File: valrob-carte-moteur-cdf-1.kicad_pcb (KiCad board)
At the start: 2 copper layers, 63 x 50 mm, 89 parts, among them J1 USB_C_Receptacle_USB2.0_14P, J2 Conn_01x02, J3 Conn_01x02, J4 Conn_01x04_Pin, J5 Conn_01x08, J6 Conn_01x02, J7 Conn_01x02, J8 Conn_01x08, J9 Conn_01x04_Pin, SW1 SW_Push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

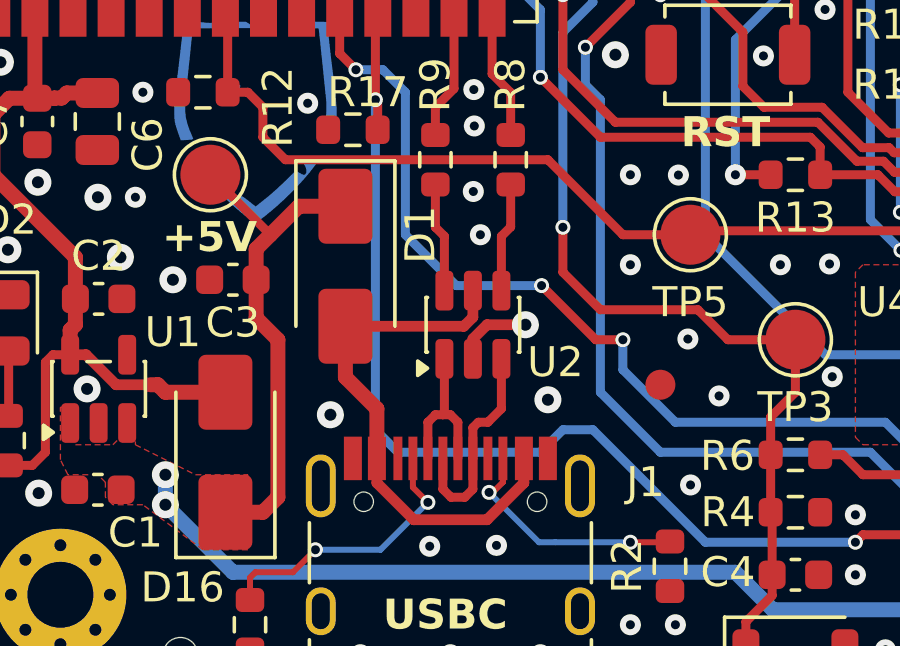
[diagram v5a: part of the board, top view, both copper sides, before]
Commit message: switch ST usb ESD to H5VU10U tvs diodes
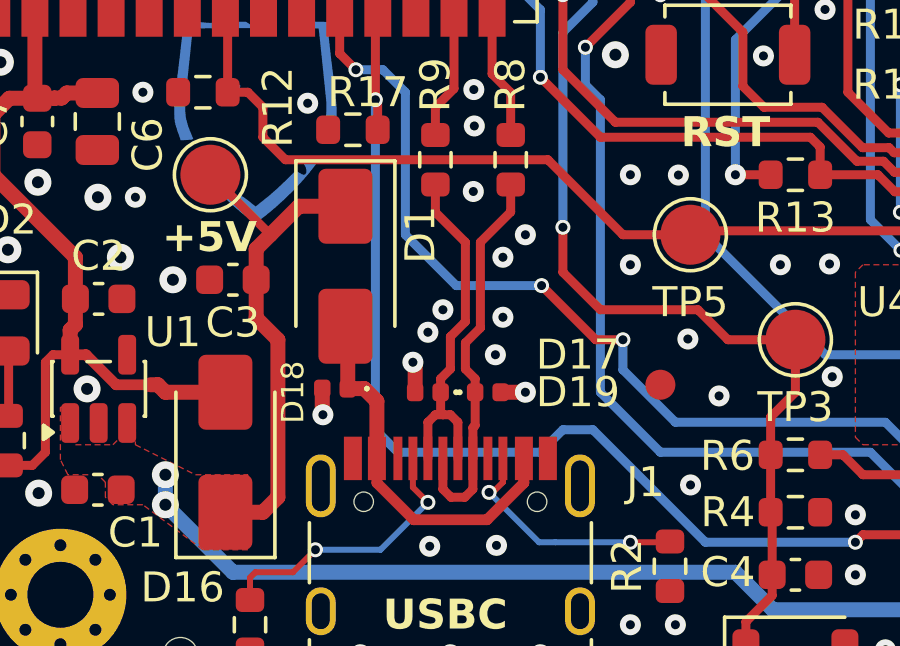
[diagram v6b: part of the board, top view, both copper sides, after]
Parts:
- removed U2: USBLC6-2SC6, Package_TO_SOT_SMD:SOT-23-6
- added D17: H5VU10U, Pers:Diode_DFN1006, F.Cu at (99.2, 124.2)
- added D18: H5VU10U, Pers:Diode_DFN1006, F.Cu at (96.2, 124.1)
- added D19: H5VU10U, Pers:Diode_DFN1006, F.Cu at (101.2, 124.2)
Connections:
- J1 pad A6: Net-(J1-D+-PadA6) -> /D+
- J1 pad A7: Net-(J1-D--PadA7) -> /D-
- J1 pad B6: Net-(J1-D+-PadA6) -> /D+
- J1 pad B7: Net-(J1-D--PadA7) -> /D-
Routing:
- net /D+: track 3.67 -> 13.2 mm
- net /D-: track 3.66 -> 12.1 mm
- net Net-(J1-D+-PadA6): track 7.17 -> 0.00 mm
- net Net-(J1-D--PadA7): track 5.50 -> 0.00 mm
- net VBUS: track 17.7 -> 12.7 mm
- net GND: track 2.61 -> 2.74 mm, vias 177 -> 182

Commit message: pcb(silkscreeen): improvements
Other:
- board text added: "1"
- board text added: "2"
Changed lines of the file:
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@@
 		(tags "connector Molex PicoBlade horizontal")
 		(property "Reference" "J8"
-			(at 11.375 -1.95 0)
+			(at 11.125 -2 0)
 			(layer "F.SilkS")
 			(effects
@@
 		)
 	)
+	(gr_text "2"
+		(at 112.5 95.5 0)
+		(layer "F.SilkS" knockout)
+		(effects
+			(font
+				(size 1 1)
+				(thickness 0.2)
+				(bold yes)
+			)
+			(justify left bottom)
+		)
+	)
 	(gr_text "+12V"
 		(at 137 97.75 90)
@@
 		)
 	)
+	(gr_text "40"
+		(at 97.84381 91.75 180)
+		(layer "F.SilkS" knockout)
+		(effects
+			(font
+				(size 0.8 0.8)
+				(thickness 0.16)
+				(bold yes)
+			)
+			(justify left bottom)
+		)
+	)
+	(gr_text "39"
+		(at 100.09381 91.75 180)
+		(layer "F.SilkS" knockout)
+		(effects
+			(font
+				(size 0.8 0.8)
+				(thickness 0.16)
+				(bold yes)
+			)
+			(justify left bottom)
+		)
+	)
+	(gr_text "41"
+		(at 95.09381 91.75 180)
+		(layer "F.SilkS" knockout)
+		(effects
+			(font
+				(size 0.8 0.8)
+				(thickness 0.16)
+				(bold yes)
+			)
+			(justify left bottom)
+		)
+	)
 	(gr_text "M1"
 		(at 124 132.25 0)
@@
 				(bold yes)
 			)
+			(justify left bottom)
+		)
+	)
+	(gr_text "42"
+		(at 92.59381 91.75 180)
+		(layer "F.SilkS" knockout)
+		(effects
+			(font
+				(size 0.8 0.8)
+				(thickness 0.16)
+				(bold yes)
+			)
+			(justify left bottom)
+		)
+	)
+	(gr_text "1"
+		(at 117.5 95.5 0)
+		(layer "F.SilkS" knockout)
+		(effects
+			(font
+				(size 1 1)
+				(thickness 0.2)
+				(bold yes)
+			)

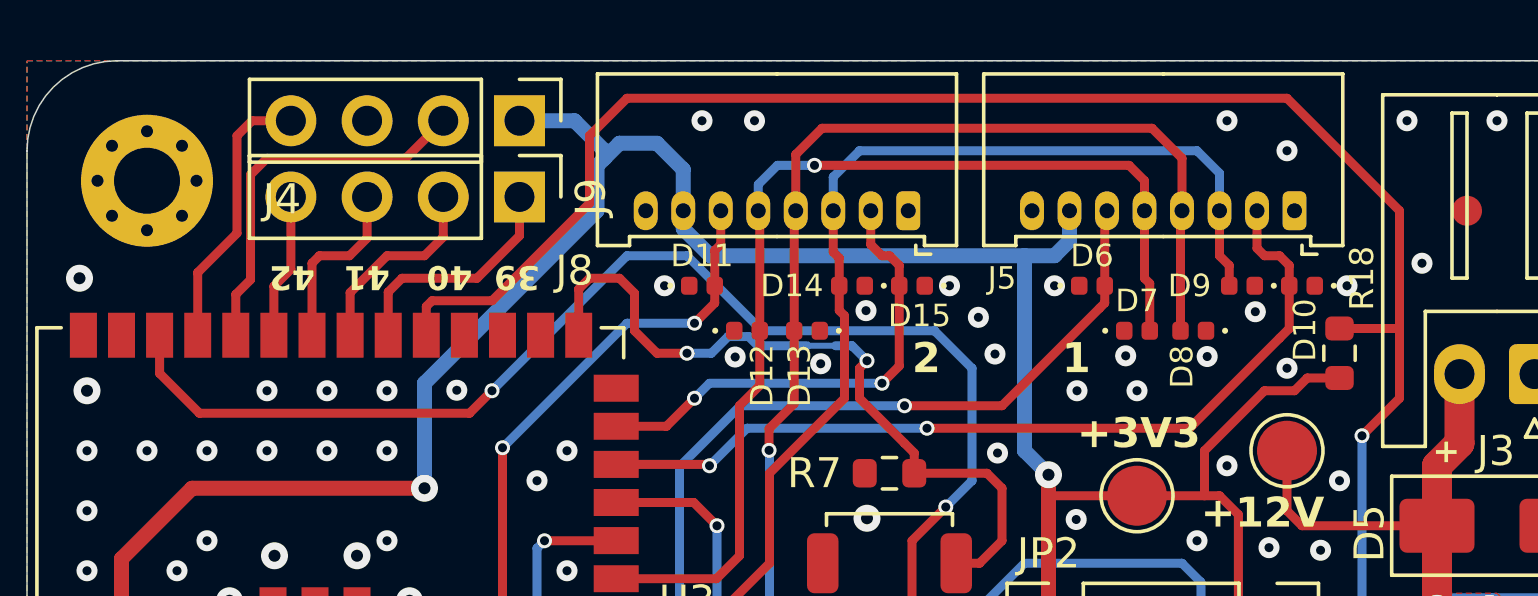
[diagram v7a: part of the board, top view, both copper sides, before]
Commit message: fix spi connectors TVS diodes polarity
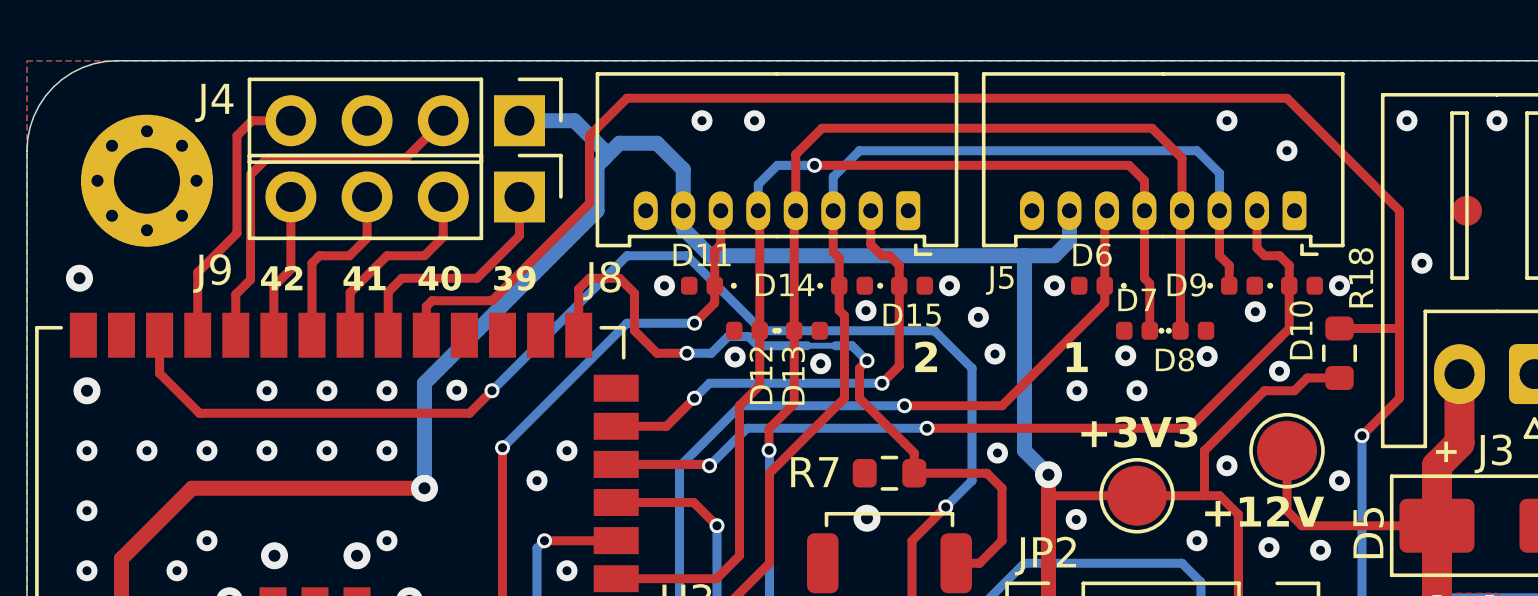
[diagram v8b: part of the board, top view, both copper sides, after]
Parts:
- turned D10 to 0 degrees
- turned D11 to 180 degrees
- turned D12 to 180 degrees
- turned D13 to 0 degrees
- turned D14 to 0 degrees
- turned D15 to 0 degrees
- turned D6 to 180 degrees
- turned D7 to 180 degrees
- turned D8 to 0 degrees
- turned D9 to 0 degrees
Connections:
- C4 pad 1: /Vsense -> +12V
- D10 pad 1: GND -> /ALERT1
- D10 pad 2: /ALERT1 -> GND
- D11 pad 1: GND -> /CS1
- D11 pad 2: /CS1 -> GND
- D12 pad 1: GND -> /MISO
- D12 pad 2: /MISO -> GND
- D13 pad 1: GND -> /MOSI
- D13 pad 2: /MOSI -> GND
- D14 pad 1: GND -> /SCLK
- D14 pad 2: /SCLK -> GND
- D15 pad 1: GND -> /ALERT2
- D15 pad 2: /ALERT2 -> GND
- D4 pad 1: /Vsense -> +12V
- D6 pad 1: GND -> /CS0
- D6 pad 2: /CS0 -> GND
- D7 pad 1: GND -> /MISO
- D7 pad 2: /MISO -> GND
- D8 pad 1: GND -> /MOSI
- D8 pad 2: /MOSI -> GND
- D9 pad 1: GND -> /SCLK
- D9 pad 2: /SCLK -> GND
- TP3 pad 1: /Vsense -> +12V
